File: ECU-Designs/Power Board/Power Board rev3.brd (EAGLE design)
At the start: 87.8 x 143.2 mm, 84 parts, among them X1 CONNECTOR-2, X2 CONNECTOR-6, X3 CONNECTOR-10MX150L_VERTICAL-10, X4 CONNECTOR-10MX150L_VERTICAL-10

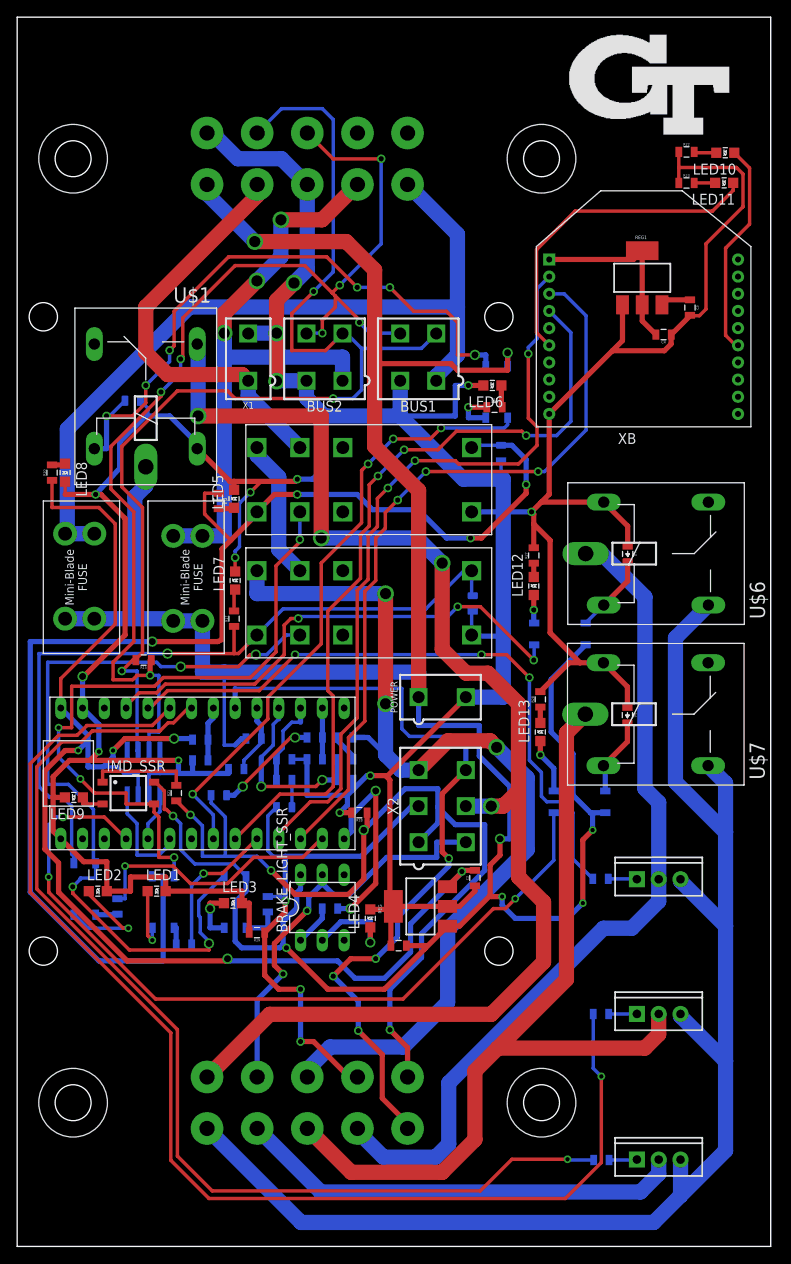
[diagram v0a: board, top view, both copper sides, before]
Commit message: New versions of power board, bspd test board, can shield, bms adapter segment, bms shield
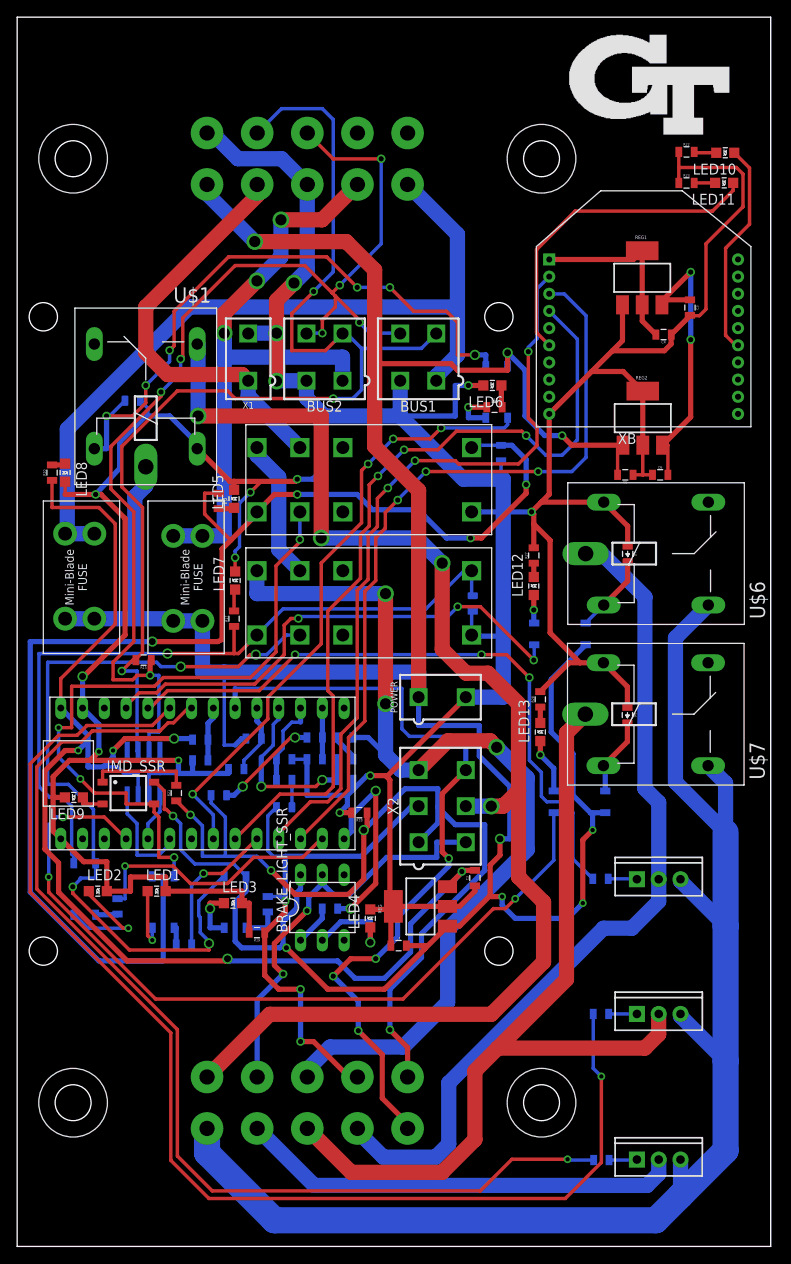
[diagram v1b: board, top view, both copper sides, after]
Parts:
- added C5: .22uF, HyTechDevices:0805
- added C6: .1uF, HyTechDevices:0805
- added REG2: 5V, HyTechDevices:SOT223
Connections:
- net +12V: now also C5.2, REG2.1
- net GND: now also C5.1, C6.1, REG2.2, REG2.4
- net N$35: now also C6.2, REG2.3
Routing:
- net N$35: track 3.50 -> 34.3 mm, vias 0 -> 2
- net +12V: track 333.0 -> 358.1 mm, vias 8 -> 9
- net GND: track 506.8 -> 525.7 mm
- net XB8: track 92.3 -> 96.5 mm
- net XBDI: track 88.2 -> 90.1 mm
- net GND1: track 164.2 -> 165.6 mm
- net FAN3-: track 52.4 -> 51.8 mm
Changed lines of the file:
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@@
 <element name="LED12" library="HyTechDevices" package="LED-805" value="" x="60.198" y="45.212"/>
 <element name="LED13" library="HyTechDevices" package="LED-805" value="" x="60.96" y="28.194"/>
+<element name="REG2" library="HyTechDevices" package="SOT223" value="5V" x="72.898" y="64.77"/>
+<element name="C5" library="HyTechDevices" package="0805" value=".22uF" x="70.866" y="58.166" rot="R180"/>
+<element name="C6" library="HyTechDevices" package="0805" value=".1uF" x="74.93" y="58.166"/>
 </elements>
 <signals>
@@
 <wire x1="78.398" y1="76.684" x2="76.224" y2="74.51" width="0.6096" layer="1"/>
 <wire x1="78.398" y1="76.684" x2="78.398" y2="76.758" width="0.6096" layer="1"/>
-<wire x1="62" y1="65.262" x2="69.362" y2="72.624" width="0.6096" layer="1"/>
+<wire x1="66.949" y1="70.211" x2="62" y2="65.262" width="0.6096" layer="1"/>
+<wire x1="66.949" y1="70.211" x2="69.362" y2="72.624" width="0.6096" layer="1"/>
 <wire x1="69.362" y1="72.624" x2="70.536" y2="73.798" width="0.6096" layer="1"/>
 <wire x1="70.536" y1="73.798" x2="70.536" y2="77.978" width="0.6096" layer="1"/>
@@
 <wire x1="61.0764" y1="54.9804" x2="62" y2="55.904" width="0.6096" layer="1"/>
 <wire x1="62" y1="55.904" x2="62" y2="65.262" width="0.6096" layer="1"/>
+<contactref element="REG2" pad="2"/>
+<contactref element="REG2" pad="4"/>
+<contactref element="C5" pad="1"/>
+<contactref element="C6" pad="1"/>
+<wire x1="72.898" y1="58.166" x2="71.766" y2="58.166" width="0.4064" layer="1"/>
+<wire x1="72.898" y1="58.166" x2="74.03" y2="58.166" width="0.4064" layer="1"/>
+<wire x1="72.898" y1="61.62" x2="72.898" y2="58.166" width="0.4064" layer="1"/>
+<wire x1="72.898" y1="61.62" x2="72.898" y2="67.92" width="0.6096" layer="1"/>
+<wire x1="72.898" y1="67.92" x2="70.607" y2="70.211" width="0.6096" layer="1"/>
+<wire x1="70.607" y1="70.211" x2="66.949" y2="70.211" width="0.6096" layer="1"/>
 <wire x1="25.273" y1="56.422" x2="25.908" y2="54.864" width="0" layer="19" extent="1-16"/>
 </signal>
@@
 <wire x1="13.716" y1="55.626" x2="13.716" y2="41.656" width="1.778" layer="16"/>
 <wire x1="13.716" y1="41.656" x2="13.462" y2="41.402" width="1.778" layer="16"/>
-<wire x1="57.15" y1="70.818" x2="57.15" y2="72.39" width="0.6096" layer="16"/>
+<wire x1="57.15" y1="72.39" x2="57.15" y2="70.818" width="0.6096" layer="16"/>
 <via x="57.15" y="72.39" extent="1-16" drill="0.8" shape="square"/>
 <wire x1="33.02" y1="11.557" x2="33.02" y2="9.906" width="0.6096" layer="16"/>
@@
 <wire x1="32.5755" y1="7.6835" x2="32.5755" y2="9.4615" width="0.6096" layer="16"/>
 <wire x1="30.988" y1="6.096" x2="32.5755" y2="7.6835" width="0.6096" layer="16"/>
+<contactref element="REG2" pad="1"/>
+<contactref element="C5" pad="2"/>
+<wire x1="69.966" y1="61.62" x2="70.598" y2="61.62" width="0.4064" layer="1"/>
+<wire x1="69.966" y1="61.62" x2="69.966" y2="58.166" width="0.4064" layer="1"/>
+<wire x1="70.598" y1="61.62" x2="64.618" y2="61.62" width="0.6096" layer="1"/>
+<wire x1="64.618" y1="61.62" x2="63.5" y2="62.738" width="0.6096" layer="1"/>
+<via x="63.5" y="62.738" extent="1-16" drill="0.6" shape="square"/>
+<wire x1="63.5" y1="62.738" x2="61.468" y2="62.738" width="0.6096" layer="16"/>
+<wire x1="61.468" y1="62.738" x2="59.182" y2="65.024" width="0.6096" layer="16"/>
+<wire x1="59.182" y1="65.024" x2="59.182" y2="70.358" width="0.6096" layer="16"/>
+<wire x1="59.182" y1="70.358" x2="57.15" y2="72.39" width="0.6096" layer="16"/>
 </signal>
 <signal name="SHUTDOWN_POWER">
@@
 <wire x1="58.801" y1="63.246" x2="59.309" y2="62.738" width="0.4064" layer="1"/>
 <via x="59.309" y="62.738" extent="1-16" drill="0.6" shape="square"/>
-<wire x1="59.309" y1="62.738" x2="62.865" y2="62.738" width="0.4064" layer="16"/>
-<wire x1="62.865" y1="62.738" x2="64.516" y2="64.389" width="0.4064" layer="16"/>
-<wire x1="64.516" y1="64.389" x2="64.516" y2="74.746" width="0.4064" layer="16"/>
-<wire x1="64.516" y1="74.746" x2="62" y2="77.262" width="0.4064" layer="16"/>
+<wire x1="59.309" y1="62.738" x2="61.595" y2="60.452" width="0.4064" layer="16"/>
+<wire x1="61.595" y1="60.452" x2="63.5" y2="60.452" width="0.4064" layer="16"/>
+<wire x1="63.5" y1="60.452" x2="65.278" y2="62.23" width="0.4064" layer="16"/>
+<wire x1="65.278" y1="62.23" x2="65.278" y2="73.984" width="0.4064" layer="16"/>
+<wire x1="65.278" y1="73.984" x2="62" y2="77.262" width="0.4064" layer="16"/>
 </signal>
 <signal name="XBDO">
@@
 <wire x1="46.355" y1="59.817" x2="51.054" y2="59.817" width="0.4064" layer="1"/>
 <wire x1="51.054" y1="59.817" x2="51.435" y2="59.436" width="0.4064" layer="1"/>
-<via x="59.563" y="72.263" extent="1-16" drill="0.6" shape="square"/>
-<wire x1="59.563" y1="64.77" x2="59.563" y2="72.263" width="0.4064" layer="1"/>
-<wire x1="59.563" y1="72.263" x2="59.563" y2="73.025" width="0.4064" layer="16"/>
+<via x="59.563" y="72.517" extent="1-16" drill="0.6" shape="square"/>
+<wire x1="59.563" y1="64.77" x2="59.563" y2="72.517" width="0.4064" layer="1"/>
+<wire x1="59.563" y1="72.517" x2="59.563" y2="73.025" width="0.4064" layer="16"/>
 <wire x1="59.563" y1="73.025" x2="60.579" y2="74.041" width="0.4064" layer="16"/>
 <wire x1="60.579" y1="74.041" x2="60.579" y2="79.841" width="0.4064" layer="16"/>
@@
 <wire x1="47.625" y1="58.547" x2="60.706" y2="58.547" width="0.4064" layer="1"/>
 <via x="60.706" y="58.547" extent="1-16" drill="0.6" shape="square"/>
-<wire x1="60.706" y1="58.547" x2="61.468" y2="58.547" width="0.4064" layer="16"/>
-<wire x1="61.468" y1="58.547" x2="66.294" y2="63.373" width="0.4064" layer="16"/>
-<wire x1="66.294" y1="63.373" x2="66.294" y2="76.708" width="0.4064" layer="16"/>
 <wire x1="66.294" y1="76.708" x2="63.754" y2="79.248" width="0.4064" layer="16"/>
 <wire x1="63.754" y1="79.248" x2="62.014" y2="79.248" width="0.4064" layer="16"/>
 <wire x1="62.014" y1="79.248" x2="62" y2="79.262" width="0.4064" layer="16"/>
+<wire x1="60.706" y1="58.547" x2="64.643" y2="58.547" width="0.4064" layer="16"/>
+<wire x1="64.643" y1="58.547" x2="66.294" y2="60.198" width="0.4064" layer="16"/>
+<wire x1="66.294" y1="60.198" x2="66.294" y2="76.708" width="0.4064" layer="16"/>
 </signal>
 <signal name="N$10">
@@
 <wire x1="75.136" y1="77.978" x2="75.716" y2="78.558" width="0.6096" layer="1"/>
 <wire x1="75.716" y1="78.558" x2="78.398" y2="78.558" width="0.6096" layer="1"/>
+<contactref element="C6" pad="2"/>
+<contactref element="REG2" pad="3"/>
+<wire x1="75.83" y1="61.62" x2="75.198" y2="61.62" width="0.4064" layer="1"/>
+<wire x1="75.83" y1="61.62" x2="75.83" y2="58.166" width="0.4064" layer="1"/>
+<wire x1="75.198" y1="61.62" x2="78.486" y2="64.908" width="0.6096" layer="1"/>
+<wire x1="78.486" y1="64.908" x2="78.486" y2="73.914" width="0.6096" layer="1"/>
+<via x="78.486" y="73.914" extent="1-16" drill="0.6" shape="square"/>
+<wire x1="78.486" y1="73.914" x2="78.486" y2="81.788" width="0.6096" layer="16"/>
+<via x="78.486" y="81.788" extent="1-16" drill="0.6" shape="square"/>
+<wire x1="78.486" y1="81.788" x2="75.136" y2="78.438" width="0.6096" layer="1"/>
+<wire x1="75.136" y1="78.438" x2="75.136" y2="77.978" width="0.6096" layer="1"/>
 </signal>
 <signal name="VCC">
@@
 <wire x1="80.51" y1="24.2776" x2="82.55" y2="22.2376" width="1.778" layer="16"/>
 <wire x1="82.55" y1="16.51" x2="82.55" y2="22.2376" width="1.778" layer="16"/>
-<wire x1="82.55" y1="5.588" x2="82.55" y2="16.51" width="1.778" layer="16"/>
-<wire x1="82.55" y1="5.588" x2="82.55" y2="-10.16" width="1.778" layer="16"/>
-<wire x1="22.126" y1="-17.9972" x2="22.0892" y2="-18.034" width="1.778" layer="16"/>
 <wire x1="76.708" y1="39.1576" x2="76.708" y2="22.352" width="1.778" layer="16"/>
 <wire x1="76.708" y1="22.352" x2="82.55" y2="16.51" width="1.778" layer="16"/>
@@
 <wire x1="77.298" y1="-4.656" x2="77.298" y2="-4.908" width="1.778" layer="16"/>
 <wire x1="77.298" y1="-4.908" x2="82.55" y2="-10.16" width="1.778" layer="16"/>
-<wire x1="82.55" y1="-20.574" x2="82.55" y2="-10.16" width="1.778" layer="16"/>
 <wire x1="77.298" y1="-21.624" x2="77.298" y2="-25.826" width="1.778" layer="16"/>
-<wire x1="77.298" y1="-25.826" x2="82.55" y2="-20.574" width="1.778" layer="16"/>
-<wire x1="77.298" y1="-25.826" x2="74.168" y2="-28.956" width="1.778" layer="16"/>
-<wire x1="74.168" y1="-28.956" x2="33.0848" y2="-28.956" width="1.778" layer="16"/>
-<wire x1="33.0848" y1="-28.956" x2="22.126" y2="-17.9972" width="1.778" layer="16"/>
+<wire x1="22.126" y1="-17.9972" x2="22.126" y2="-20.856" width="3.048" layer="16"/>
+<wire x1="22.126" y1="-20.856" x2="29.972" y2="-28.702" width="3.048" layer="16"/>
+<wire x1="29.972" y1="-28.702" x2="74.422" y2="-28.702" width="3.048" layer="16"/>
+<wire x1="74.422" y1="-28.702" x2="77.298" y2="-25.826" width="3.048" layer="16"/>
+<wire x1="77.298" y1="-25.826" x2="82.55" y2="-20.574" width="3.048" layer="16"/>
+<wire x1="82.55" y1="-20.574" x2="82.55" y2="-10.16" width="3.048" layer="16"/>
+<wire x1="82.55" y1="-10.16" x2="82.55" y2="5.588" width="3.048" layer="16"/>
+<wire x1="82.55" y1="5.588" x2="82.55" y2="16.51" width="3.048" layer="16"/>
 </signal>
 <signal name="FAN1-">
@@
 <contactref element="X3" pad="9"/>
 <wire x1="74.758" y1="-21.624" x2="74.758" y2="-23.286" width="1.778" layer="16"/>
-<wire x1="72.644" y1="-25.4" x2="35.3708" y2="-25.4" width="1.778" layer="16"/>
-<wire x1="74.758" y1="-23.286" x2="72.644" y2="-25.4" width="1.778" layer="16"/>
-<wire x1="35.3708" y1="-25.4" x2="27.968" y2="-17.9972" width="1.778" layer="16"/>
+<wire x1="74.758" y1="-23.286" x2="73.406" y2="-24.638" width="1.778" layer="16"/>
+<wire x1="73.406" y1="-24.638" x2="34.6088" y2="-24.638" width="1.778" layer="16"/>
+<wire x1="34.6088" y1="-24.638" x2="27.968" y2="-17.9972" width="1.778" layer="16"/>
 </signal>
 <signal name="N$4">

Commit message: Updated external diagram accumulator connector, add power board resistor values, add numbers to 16pin connector symbol
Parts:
- R22: value (none) -> 82
- R23: value (none) -> 20
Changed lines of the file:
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@@
 <?xml version="1.0" encoding="utf-8"?>
 <!DOCTYPE eagle SYSTEM "eagle.dtd">
-<eagle version="8.1.0">
+<eagle version="8.2.1">
 <drawing>
 <settings>
@@
 <element name="XB" library="HyTechDevices" package="XBEE" value="XBEE" x="73" y="77.762"/>
 <element name="LED10" library="HyTechDevices" package="LED-805" value="" x="82.514" y="95.696" rot="R90"/>
-<element name="R22" library="HyTechDevices" package="0805" value="" x="77.996" y="95.794"/>
+<element name="R22" library="HyTechDevices" package="0805" value="82" x="77.996" y="95.794"/>
 <element name="LED11" library="HyTechDevices" package="LED-805" value="" x="82.386" y="92.188" rot="R90"/>
-<element name="R23" library="HyTechDevices" package="0805" value="" x="77.996" y="92.176"/>
+<element name="R23" library="HyTechDevices" package="0805" value="20" x="77.996" y="92.176"/>
 <element name="REG1" library="HyTechDevices" package="SOT223" value="TLV1117LV33" x="72.836" y="81.128"/>
 <element name="C3" library="HyTechDevices" package="0805" value="1uF" x="78.398" y="77.658" rot="R270"/>
